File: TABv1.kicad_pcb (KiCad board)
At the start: 4 copper layers, 90 x 45 mm, 147 parts, among them IC1 TPS630702RNMR, J10 Conn_02x03_Odd_Even, J11 Conn_UART_1, J15 DB141R-2.54-8P-GN, J4 Conn_Coaxial, J5 Conn_02x06_Counter_Clockwise, J6 SWD, J7 503398-1892, J8 1053141104, J9 Conn_02x03_Odd_Even, Q1 MJD44H11T4G, Q10 PJM09P30DF, Q11 PJM09P30DF, Q12 PJM09P30DF, Q13 PJM09P30DF, Q2 NMOS, Q4 BC817-25,215, Q5 NMOS, Q6 NMOS, Q7 NMOS, Q8 NMOS, Q9 NMOS, SW1 BOOTSEL, SW2 RESET, U1 RP2350B-QFN80, U10 RAK3172, U11 LPS22DF, U2 W25Q128JVS, U4 LSM6DSV80XTR, U5 LSM6DSV80XTR, U7 LM334M, U8 LIS2MDL, U9 TESEO-LIV4F, Y1 12MHz

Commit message: perché non funziona
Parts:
- removed J15: DB141R-2.54-8P-GN, DB141R-2-54-8:CONN16_DB141R_DIO
- removed Q13: PJM09P30DF, easyeda2kicad:DFN-6_L2.0-W2.0-P0.65-BL-EP-1
- removed Q9: NMOS, Package_TO_SOT_SMD:SOT-23_Handsoldering
- removed R35, R37: 1k, Resistor_SMD:R_0603_1608Metric_Pad0.98x0.95mm_HandSolder
- removed R36, R38: 10k, Resistor_SMD:R_0603_1608Metric_Pad0.98x0.95mm_HandSolder
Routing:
- net /PYRO_FIRE_4: track 48.1 -> 0.00 mm, vias 2 -> 0
- net /Pyro/PYRO2: track 18.7 -> 1.84 mm
- net /Pyro/PYRO1: track 8.39 -> 0.00 mm
- net /Pyro/PYRO3: track 8.06 -> 0.00 mm
- net /Pyro/PYRO4: track 7.66 -> 0.00 mm
- net Net-(Q9-D): track 4.45 -> 0.00 mm
- net Net-(Q13-G): track 4.32 -> 0.00 mm
- net Net-(Q9-G): track 4.06 -> 0.00 mm
- net Net-(Q9-S): track 2.77 -> 0.00 mm
- net /Pyro/PYRO_HIGH: track 25.7 -> 23.7 mm, vias 7 -> 6
- net GND: vias 166 -> 165

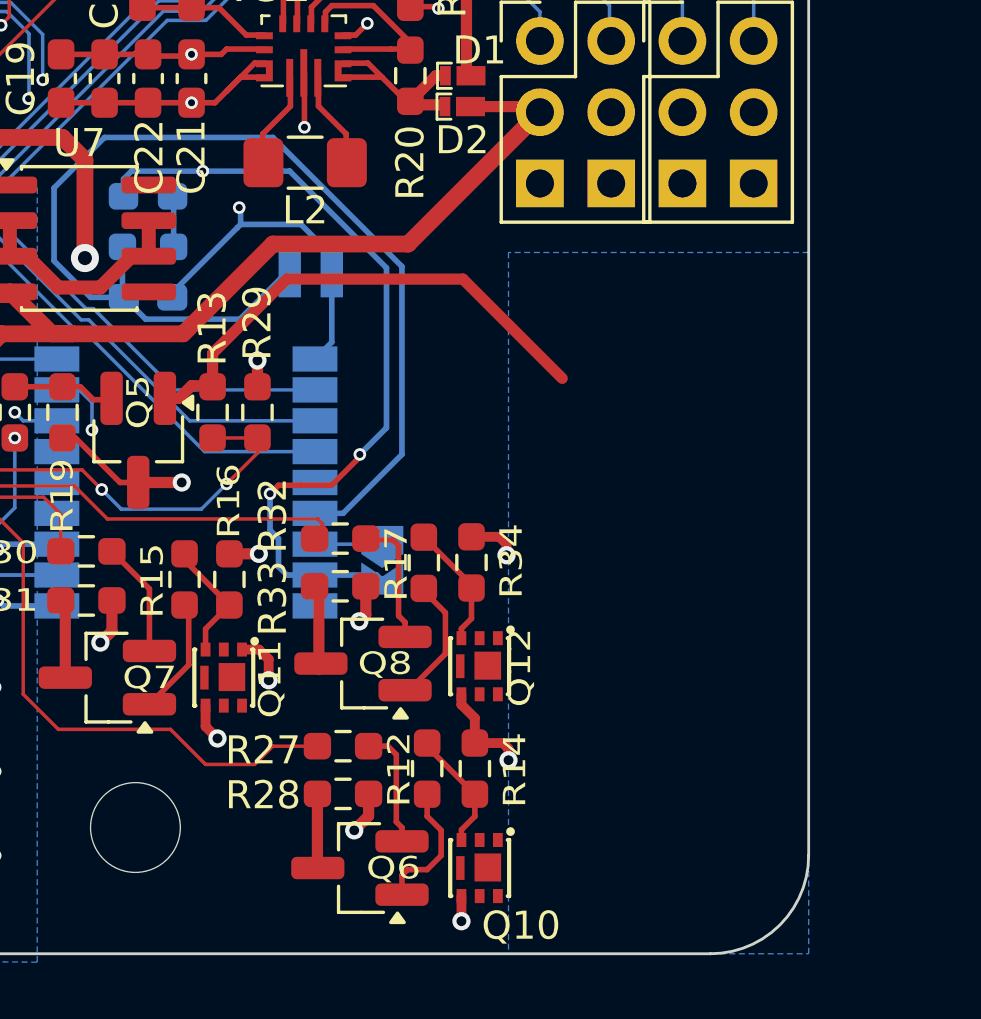
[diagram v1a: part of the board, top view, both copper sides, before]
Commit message: spostamento connettori
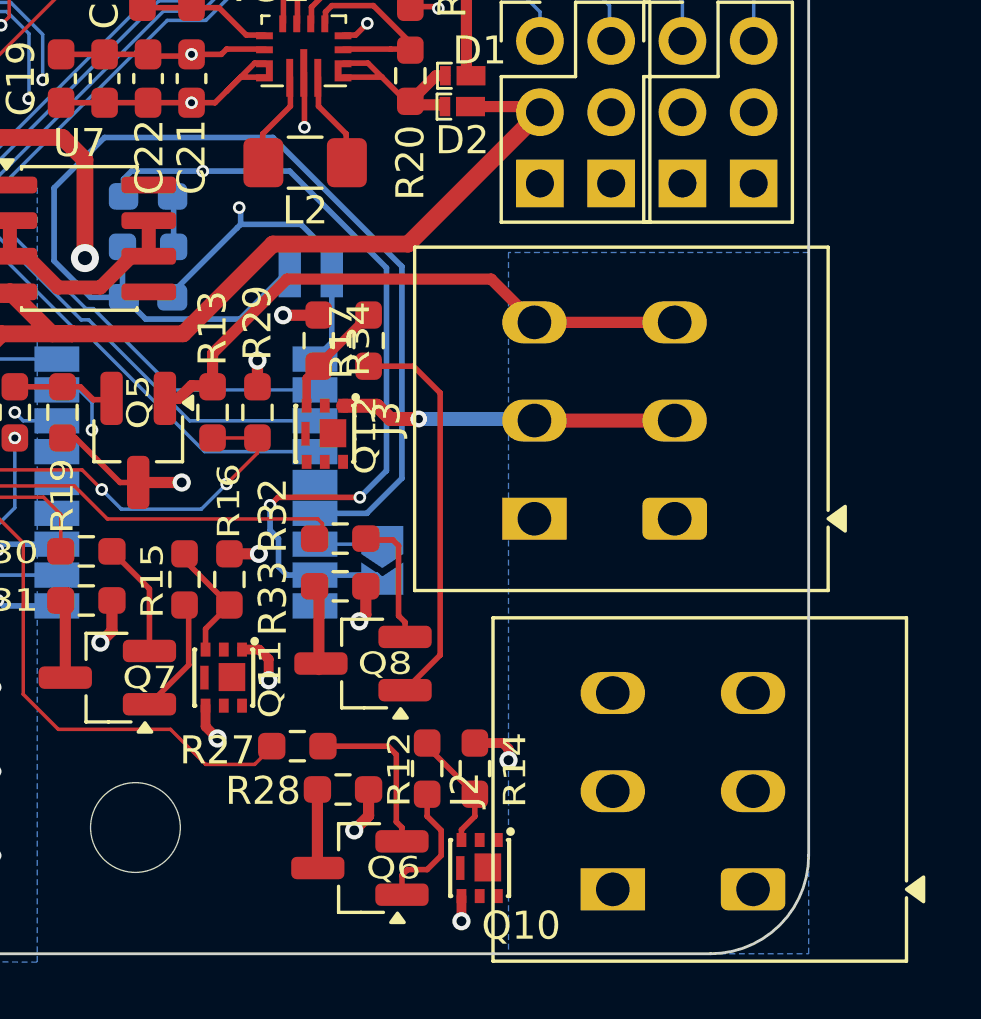
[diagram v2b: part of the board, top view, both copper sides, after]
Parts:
- added J2: Conn_01x03_Socket, TerminalBlock_WAGO:TerminalBlock_WAGO_2601-1103_1x03_P3.50mm_Horizontal, F.Cu at (160.5, 76.2)
- added J3: Conn_01x03_Socket, TerminalBlock_WAGO:TerminalBlock_WAGO_2601-1103_1x03_P3.50mm_Horizontal, F.Cu at (157.7, 63.0)
- moved Q12 9.96 mm to (145.2, 60.0)
- moved R34 9.60 mm to (145.0, 56.6)
- moved R17 8.16 mm to (146.8, 56.6)
- moved R27 1.63 mm to (144.3, 71.1)
- moved R28 0.16 mm to (145.9, 72.6)
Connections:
- U1 pad 48: /PYRO_FIRE_4 -> unconnected-(U1-GPIO39-Pad48)
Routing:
- net /Pyro/PYRO3: track 0.00 -> 12.0 mm, vias 0 -> 1
- net Net-(Q8-D): track 4.89 -> 14.1 mm
- net /Pyro/PYRO_LOW: track 18.1 -> 21.3 mm
- net /Pyro/PYRO_HIGH: track 23.7 -> 21.0 mm
- net Net-(Q6-G): track 4.29 -> 5.92 mm
- net /PYRO_FIRE_1: track 52.1 -> 50.5 mm
- net +3V3: track 179.3 -> 179.9 mm

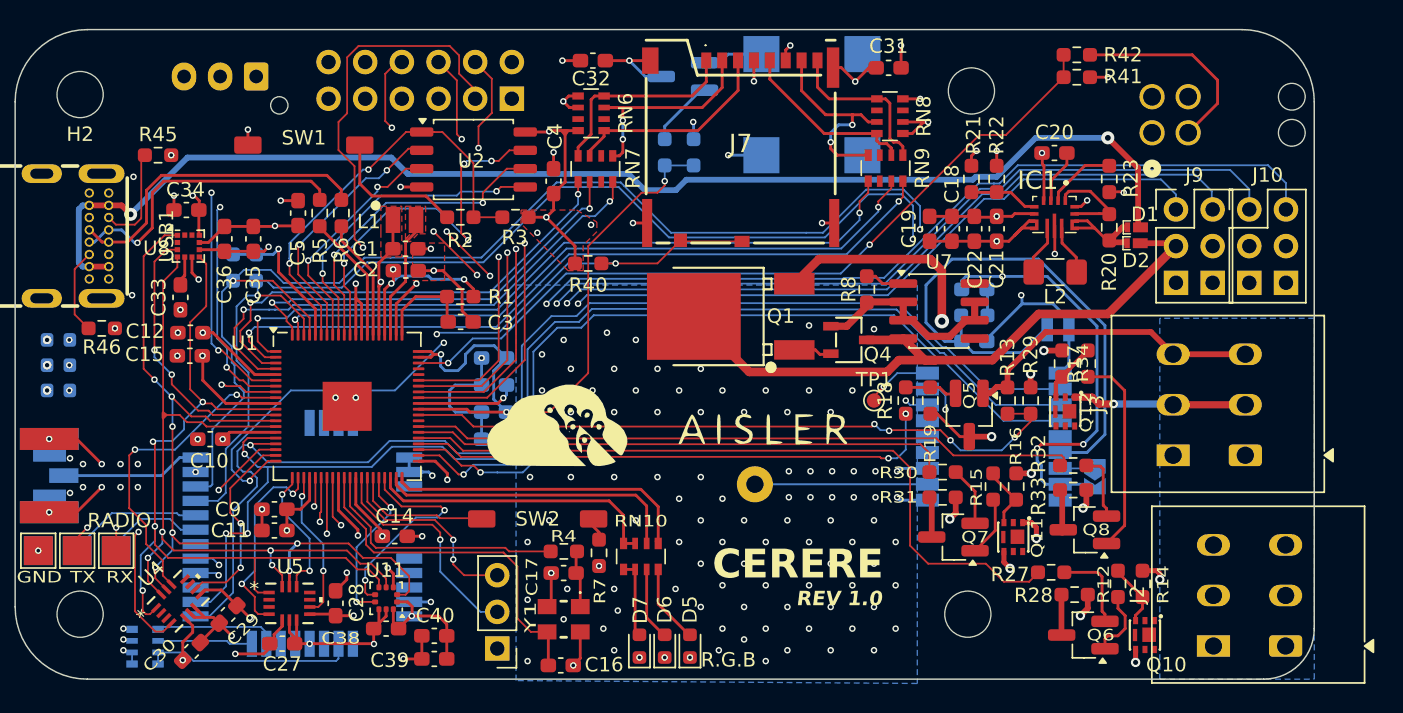
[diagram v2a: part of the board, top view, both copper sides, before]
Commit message: connettori adattati
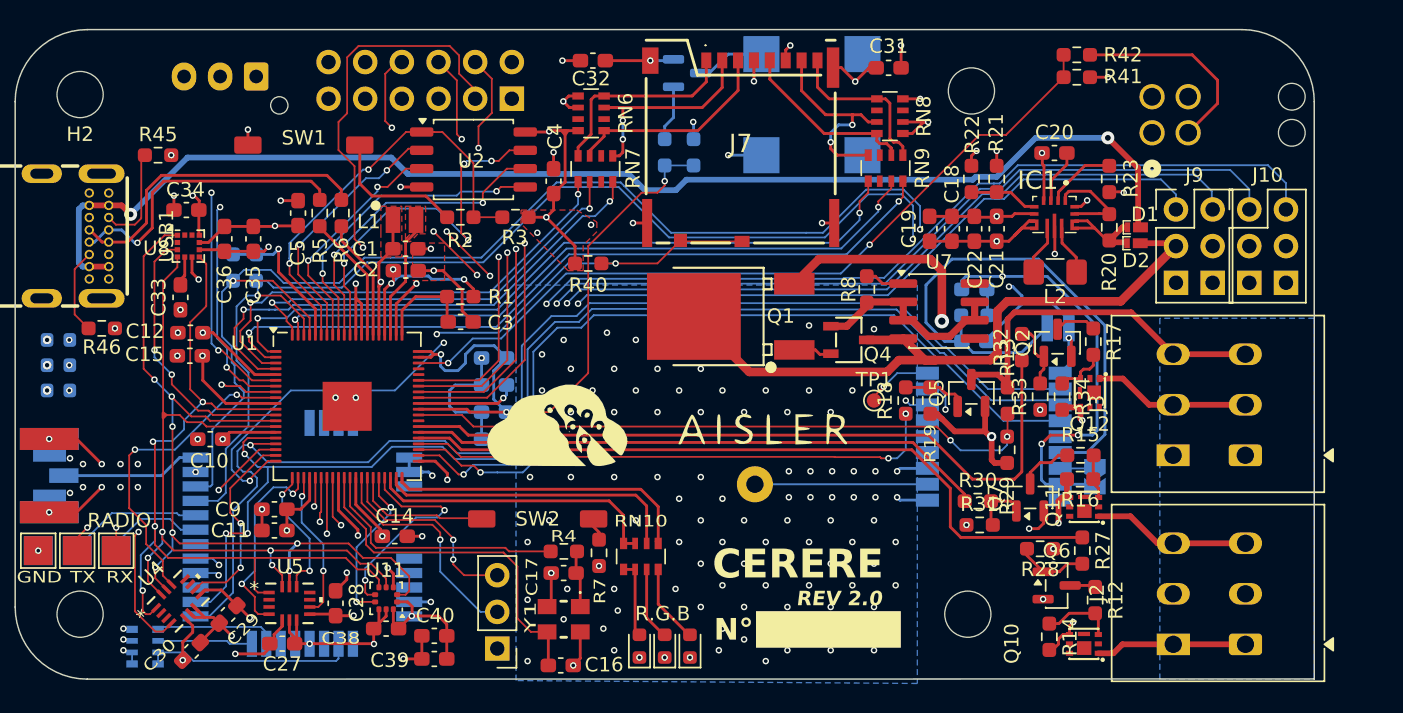
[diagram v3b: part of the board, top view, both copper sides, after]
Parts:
- removed Q8: NMOS, Package_TO_SOT_SMD:SOT-23_Handsoldering
- added Q3: DMN2040U, Package_TO_SOT_SMD:SOT-23, B.Cu at (119.0, 36.5)
- Q2: value NMOS -> DMN2040U; footprint Package_TO_SOT_SMD:SOT-23_Handsoldering -> Package_TO_SOT_SMD:SOT-23; moved to F.Cu
- Q5, Q6, Q7: value NMOS -> DMN2040U; footprint Package_TO_SOT_SMD:SOT-23_Handsoldering -> Package_TO_SOT_SMD:SOT-23
- R18, R27, R30, R32: value 1k -> 100
- moved Q2 31.8 mm to (144.7, 55.2), turned to 90 degrees
- moved R32 8.94 mm to (142.2, 55.5), turned to 90 degrees
- moved R14 7.42 mm to (144.1, 75.6), turned to -90 degrees
- moved R33 6.87 mm to (143.5, 58.9), turned to 90 degrees
- moved R15 6.43 mm to (146.3, 63.0), turned to 0 degrees
- moved Q7 5.98 mm to (142.8, 65.9), turned to 90 degrees
- moved Q11 5.36 mm to (146.6, 66.5), turned to 90 degrees
- moved R16 4.46 mm to (146.3, 64.6), turned to 180 degrees
- moved Q10 4.25 mm to (146.5, 76.0), turned to 90 degrees
- moved R28 3.97 mm to (143.5, 69.5)
- moved Q6 3.90 mm to (144.7, 72.0), turned to 0 degrees
- moved R29 3.78 mm to (141.2, 62.6), turned to 90 degrees
- moved R31 3.20 mm to (139.3, 67.8), turned to 0 degrees
- moved R30 3.16 mm to (139.2, 66.2)
- moved J2 2.79 mm to (157.7, 76.1)
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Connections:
- LS1 pad N: Net-(Q2-D) -> Net-(Q3-D)
- Q2 pad 1: Net-(Q2-D) -> Net-(Q2-G)
- Q2 pad 2: Net-(Q2-G) -> GND
- Q2 pad 3: GND -> Net-(Q2-D)
- Q5 pad 1: /Pyro/PYRO_LOW -> Net-(Q5-G)
- Q5 pad 2: Net-(Q5-G) -> GND
- Q5 pad 3: GND -> /Pyro/PYRO_LOW
- Q6 pad 1: Net-(Q6-D) -> Net-(Q6-G)
- Q6 pad 2: Net-(Q6-G) -> GND
- Q6 pad 3: Net-(Q6-S) -> Net-(Q6-D)
- Q7 pad 1: Net-(Q7-D) -> Net-(Q7-G)
- Q7 pad 2: Net-(Q7-G) -> GND
- Q7 pad 3: Net-(Q7-S) -> Net-(Q7-D)
- R10 pad 2: Net-(Q2-G) -> Net-(Q3-G)
- R17 pad 1: Net-(Q8-D) -> Net-(Q2-D)
- R28 pad 2: Net-(Q6-S) -> Net-(Q6-G)
- R31 pad 2: Net-(Q7-S) -> Net-(Q7-G)
- R32 pad 2: Net-(Q8-G) -> Net-(Q2-G)
- R33 pad 2: Net-(Q8-S) -> Net-(Q2-G)
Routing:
- net Net-(Q8-D): track 14.1 -> 0.00 mm
- net /Pyro/PYRO1: track 0.00 -> 10.4 mm
- net /Pyro/PYRO2: track 1.84 -> 11.0 mm, vias 1 -> 0
- net /PYRO_FIRE_3: track 46.3 -> 51.2 mm
- net Net-(Q8-G): track 4.62 -> 0.00 mm
- net /Pyro/PYRO_LOW: track 21.3 -> 25.7 mm
- net Net-(Q3-D): track 0.00 -> 4.33 mm
- net Net-(Q3-G): track 0.00 -> 3.88 mm
- net Net-(Q8-S): track 3.04 -> 0.00 mm
- net Net-(Q6-D): track 4.78 -> 1.77 mm
- net Net-(Q7-S): track 2.82 -> 0.00 mm
- net /Pyro/PYRO_HIGH: track 21.0 -> 23.8 mm, vias 6 -> 4
- net /PYRO_FIRE_2: track 37.3 -> 40.1 mm
- net Net-(Q6-S): track 2.65 -> 0.00 mm
- net /PYRO_SENSE: track 46.6 -> 44.1 mm, vias 4 -> 2
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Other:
- outline, holes or cut-outs redrawn
- board text added: "N°"
- board text added: "REV 2.0"
- board text removed: "REV 1.0"

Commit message: aggiornamenti rev 1.1
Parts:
- removed J6: SWD, Connector_PinHeader_2.54mm:PinHeader_1x03_P2.54mm_Vertical
- added TP10: TestPoint_Flag, TestPoint:TestPoint_Pad_2.0x2.0mm, F.Cu at (105.5, 70.5)
- added TP11: TestPoint_Flag, TestPoint:TestPoint_Pad_2.0x2.0mm, F.Cu at (102.5, 73.9)
- added TP12: TestPoint_Flag, TestPoint:TestPoint_Pad_2.0x2.0mm, F.Cu at (102.4, 70.5)
- added TP8: TestPoint_Flag, TestPoint:TestPoint_Pad_2.0x2.0mm, F.Cu at (105.5, 73.9)
- added TP9: TestPoint_Flag, TestPoint:TestPoint_Pad_2.0x2.0mm, F.Cu at (105.5, 76.9)
- J2, J3: moved to B.Cu
- L2: footprint Inductor_SMD:L_1206_3216Metric_Pad1.42x1.75mm_HandSolder -> Inductor_SMD:L_1008_2520Metric
- USB1: footprint TYPEC-306DDW-ARP16:USB-C-TH_TYPEC-306DDW-ARP16 -> BXCONN UC23-0B16F00P11:USB-C-TH_UC23-0B16F00P11
- moved J2 7.04 mm to (157.8, 69.0), turned to -90 degrees
- moved J3 6.99 mm to (157.8, 56.0), turned to -90 degrees
- moved JP1 6.98 mm to (144.3, 70.8), turned to 180 degrees
- moved C40 0.70 mm to (101.5, 76.2)
- moved C39 0.60 mm to (101.5, 77.7)
- moved USB1 0.13 mm to (76.8, 47.8)
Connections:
- J2 pad 1: /Pyro/PYRO1 -> /Pyro/PYRO2
- J2 pad 3: /Pyro/PYRO2 -> /Pyro/PYRO1
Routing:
- net +3V3: track 179.6 -> 186.2 mm
- net Net-(JP1-A): track 2.46 -> 8.18 mm
- net /RESET: track 9.03 -> 12.4 mm
- net Net-(U1-SWDIO): track 13.8 -> 11.0 mm
- net /XOUT: track 17.8 -> 20.6 mm
- net Net-(U1-SWCLK): track 15.9 -> 13.7 mm, vias 1 -> 2
- net GND: track 144.7 -> 146.7 mm, vias 165 -> 166
- net /XIN: track 24.8 -> 24.0 mm
- net ANT: vias 0 -> 1
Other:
- board text added: "BOOTSEL"
- board text added: "CH1"
- board text added: "CH2"
- board text added: "CH3"
- board text added: "DAJE"
- board text added: "PYRO"
- board text added: "RESET"
- board text added: "REV 1.1"
- board text removed: "REV 2.0"

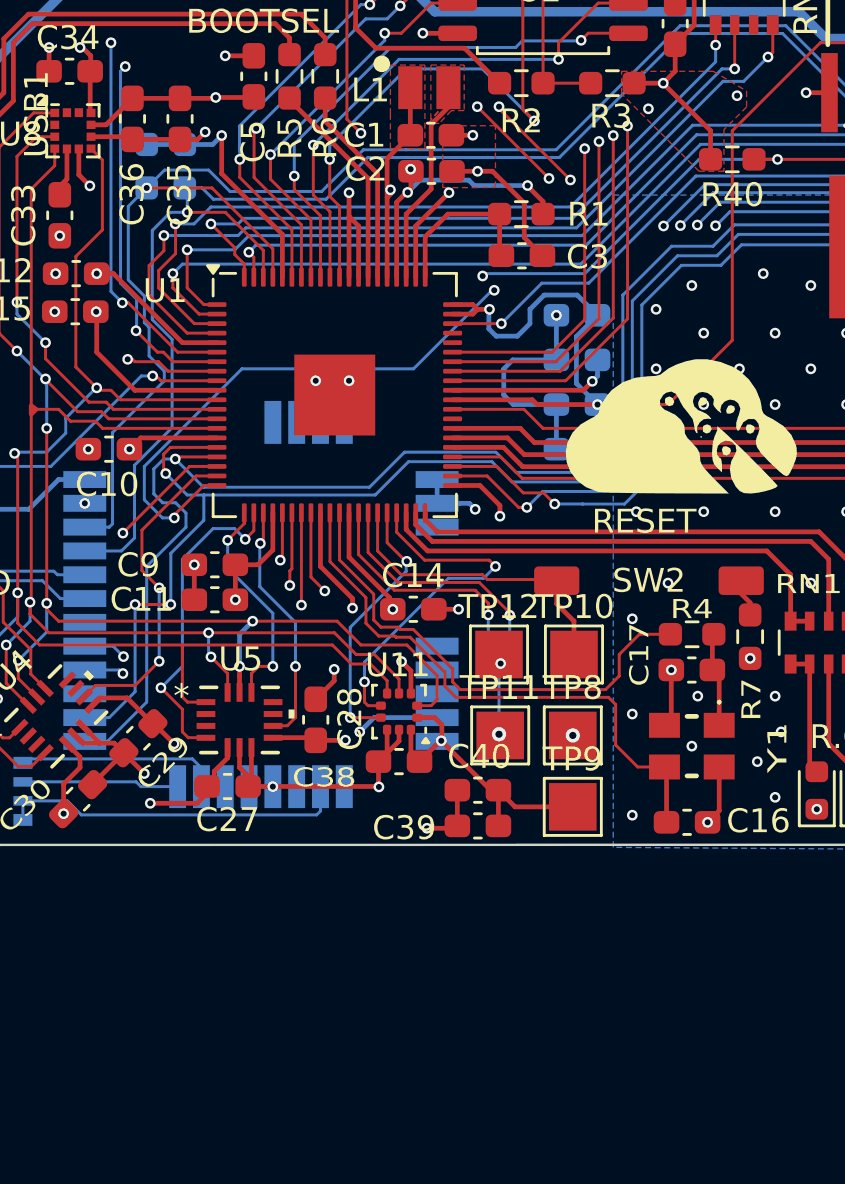
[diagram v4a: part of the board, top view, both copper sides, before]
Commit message: fpc connector inizio
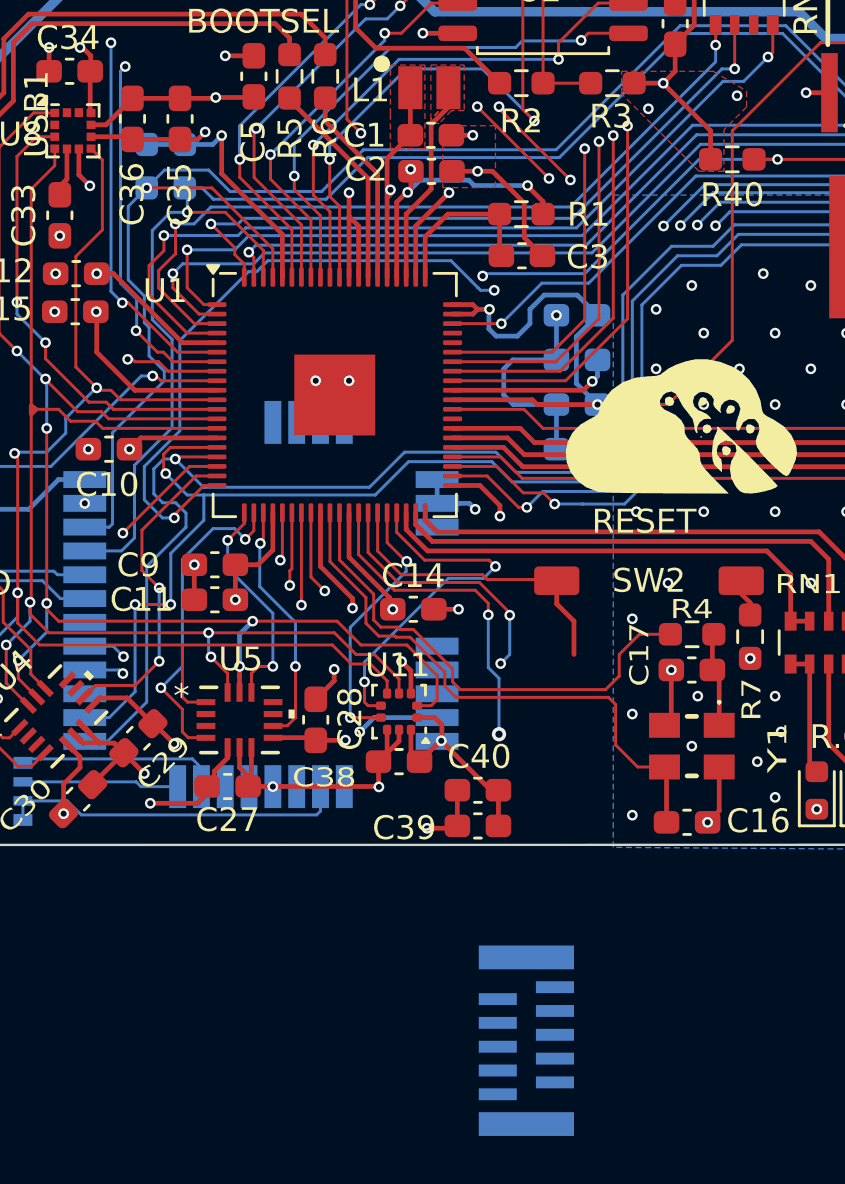
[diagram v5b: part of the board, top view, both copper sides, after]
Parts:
- removed TP10, TP11, TP12, TP8, TP9: TestPoint_Flag, TestPoint:TestPoint_Pad_2.0x2.0mm
- added J6: Conn_01x10_Socket, easyeda2kicad:FPC-SMD_XUNPU_FPC-0.5AD-10PB, B.Cu at (103.5, 86.7)
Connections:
- J7 pad 10: /SD_detect -> +3V3
- R40 pad 1: +3V3 -> GND
- U10 pad 4: Net-(U10-PB6/UART1_TX) -> /UART1_TX_RADIO
- U10 pad 5: Net-(U10-PB7/UART1_RX) -> /UART1_RX_RADIO
- U10 pad 7: /LoRa & GPS/SWDIO -> /SWDIO_RADIO
- U10 pad 8: /LoRa & GPS/SWCLK -> /SWDCLK_RADIO
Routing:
- net +3V3: track 186.2 -> 182.8 mm
- net /GPIO20: track 59.5 -> 62.7 mm
- net GND: vias 166 -> 165
